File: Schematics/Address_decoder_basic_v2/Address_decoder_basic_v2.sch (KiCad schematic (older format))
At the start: 6 parts, among them J1 Address bus, J2 Clock, J3 ROM select, J4 RAM select, J5 VIA1 select, U1 74HC00

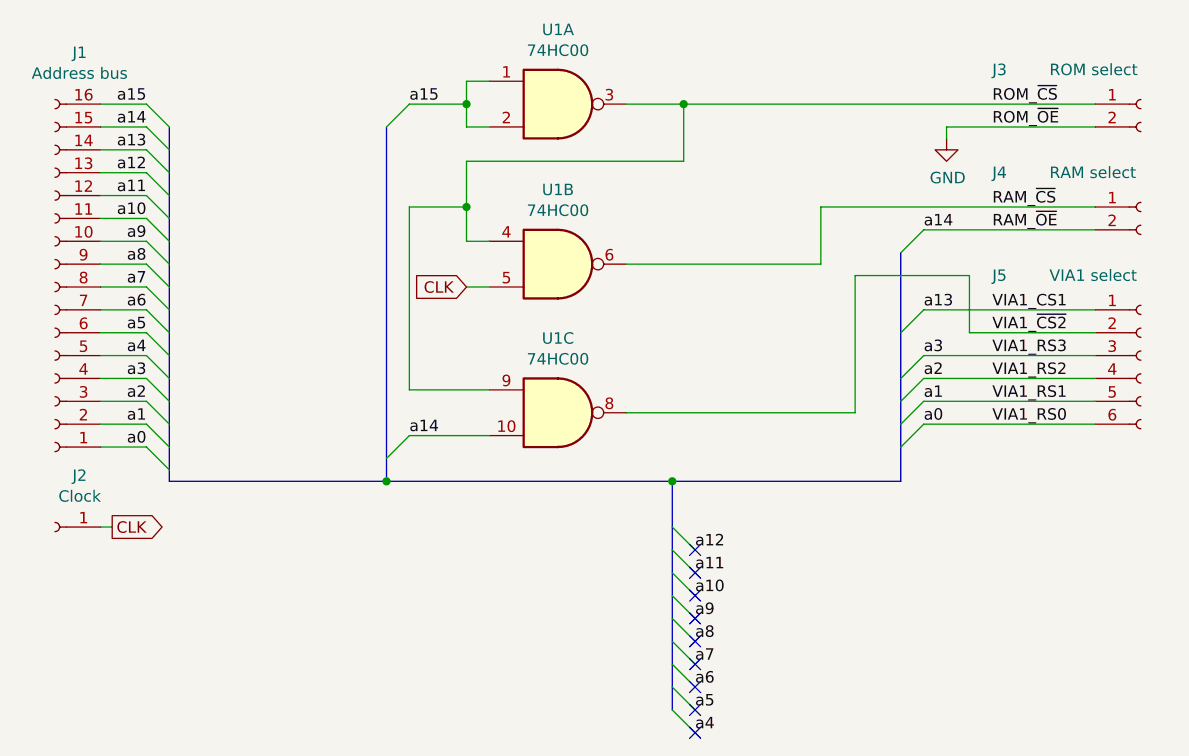
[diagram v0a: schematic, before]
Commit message: Updated v2 decoder schematic
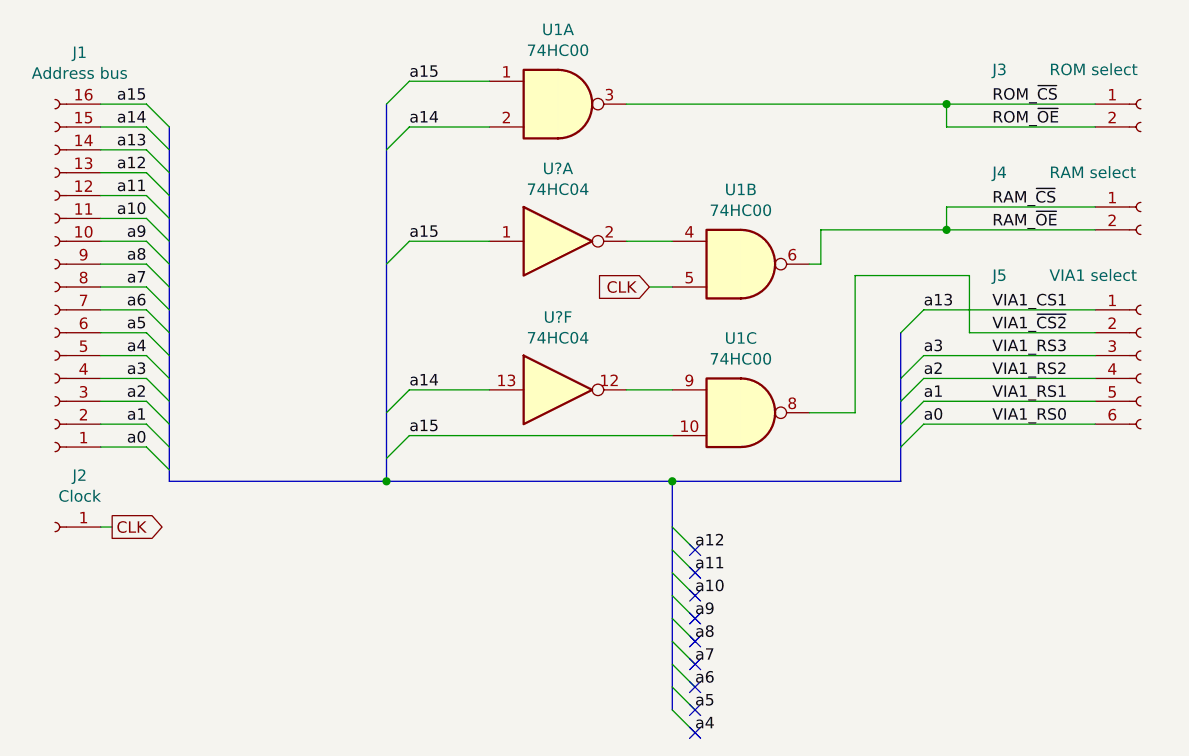
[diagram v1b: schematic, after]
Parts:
- added U? (x2): 74HC04, symbol 74xx:74HC04
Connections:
- net GND is gone; now on net ROM_~CS: J3.2 (Pin_2)
- net RAM_~CS: now also J4.2 (Pin_2)
- net ROM_~CS: no longer U1.4, U1.9
- net a15: now also U1.10, U?.1; no longer U1.2
- removed net RAM_~OE: J1.15 (Pin_15), J4.2 (Pin_2), U1.10
- new net: U1.4, U?.2
- new net: U1.9, U?.12
- new net a14: J1.15 (Pin_15), U1.2, U?.13
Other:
- moved on the sheet: U1B, U1C
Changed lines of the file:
@@
 Text Label 7400 4200 0    50   ~ 0
 VIA1_RS0
-Text Label 4850 2800 0    50   ~ 0
+Text Label 4850 3400 0    50   ~ 0
 a15
-Text Label 7100 3350 0    50   ~ 0
-a14
-$Comp
-L power:GND #PWR01
-U 1 1 5E0C3EF2
-P 7200 2950
-F 0 "#PWR01" H 7200 2700 50  0001 C CNN
-F 1 "GND" H 7205 2777 50  0000 C CNN
-F 2 "" H 7200 2950 50  0001 C CNN
-F 3 "" H 7200 2950 50  0001 C CNN
-	1    7200 2950
-	1    0    0    -1
-$EndComp
 Wire Wire Line
 	7200 2900 7850 2900
@@
 	1    0    0    -1
 $EndComp
-Wire Wire Line
-	5100 2800 5100 2900
-Wire Wire Line
-	5100 2900 5200 2900
-Wire Wire Line
-	5200 2700 5100 2700
-Wire Wire Line
-	5100 2700 5100 2800
-Connection ~ 5100 2800
-Wire Wire Line
-	7200 2900 7200 2950
-Entry Wire Line
-	4750 2900 4850 2800
+Entry Wire Line
+	4750 3500 4850 3400
 $Comp
 L 74xx:74HC00 U1
 U 2 1 5E0D5C1A
-P 5500 3500
-F 0 "U1" H 5500 3825 50  0000 C CNN
-F 1 "74HC00" H 5500 3734 50  0000 C CNN
-F 2 "" H 5500 3500 50  0001 C CNN
-F 3 "http://www.ti.com/lit/gpn/sn74hc00" H 5500 3500 50  0001 C CNN
-	2    5500 3500
+P 6300 3500
+F 0 "U1" H 6300 3825 50  0000 C CNN
+F 1 "74HC00" H 6300 3734 50  0000 C CNN
+F 2 "" H 6300 3500 50  0001 C CNN
+F 3 "http://www.ti.com/lit/gpn/sn74hc00" H 6300 3500 50  0001 C CNN
+	2    6300 3500
 	1    0    0    -1
 $EndComp
@@
 Wire Wire Line
 	7100 3900 7850 3900
-Wire Wire Line
-	5800 2800 6050 2800
-Wire Wire Line
-	6050 2800 6050 3050
-Wire Wire Line
-	6050 3050 5100 3050
-Wire Wire Line
-	5100 3050 5100 3250
-Wire Wire Line
-	5100 3400 5200 3400
-Connection ~ 6050 2800
-Wire Wire Line
-	6050 2800 7850 2800
-Text GLabel 5100 3600 0    50   Input ~ 0
+Text GLabel 5900 3600 0    50   Input ~ 0
 CLK
 Wire Wire Line
-	5100 3600 5200 3600
-Wire Wire Line
-	7100 3350 7850 3350
-Wire Wire Line
-	5800 3500 6650 3500
-Wire Wire Line
-	6650 3500 6650 3250
-Wire Wire Line
-	6650 3250 7850 3250
-Entry Wire Line
-	7000 3450 7100 3350
+	5900 3600 6000 3600
+Wire Wire Line
+	6600 3500 6650 3500
 Text Label 4850 4250 0    50   ~ 0
-a14
+a15
 $Comp
 L 74xx:74HC00 U1
 U 3 1 5E0E594E
-P 5500 4150
-F 0 "U1" H 5500 4475 50  0000 C CNN
-F 1 "74HC00" H 5500 4384 50  0000 C CNN
-F 2 "" H 5500 4150 50  0001 C CNN
-F 3 "http://www.ti.com/lit/gpn/sn74hc00" H 5500 4150 50  0001 C CNN
-	3    5500 4150
+P 6300 4150
+F 0 "U1" H 6300 4475 50  0000 C CNN
+F 1 "74HC00" H 6300 4384 50  0000 C CNN
+F 2 "" H 6300 4150 50  0001 C CNN
+F 3 "http://www.ti.com/lit/gpn/sn74hc00" H 6300 4150 50  0001 C CNN
+	3    6300 4150
 	1    0    0    -1
 $EndComp
@@
 	4750 4350 4850 4250
 Wire Wire Line
-	4850 4250 5200 4250
-Wire Wire Line
-	5200 4050 4850 4050
-Wire Wire Line
-	4850 4050 4850 3250
-Wire Wire Line
-	4850 3250 5100 3250
-Connection ~ 5100 3250
-Wire Wire Line
-	5100 3250 5100 3400
-Text Label 7100 3700 0    50   ~ 0
-a13
-Entry Wire Line
-	7000 3800 7100 3700
-Wire Wire Line
-	7100 3700 7850 3700
-Wire Wire Line
-	5800 4150 6800 4150
+	4850 4250 6000 4250
+Wire Wire Line
+	6000 4050 5800 4050
+Wire Wire Line
+	6600 4150 6800 4150
 Wire Bus Line
 	3800 4450 4750 4450
-Wire Wire Line
-	4850 2800 5100 2800
 Connection ~ 4750 4450
 Wire Bus Line
 	4750 4450 6000 4450
-Wire Wire Line
-	6800 4150 6800 3550
-Wire Wire Line
-	6800 3550 7300 3550
-Wire Wire Line
-	7300 3550 7300 3800
-Wire Wire Line
-	7300 3800 7850 3800
 Text Label 6100 4750 0    50   ~ 0
 a12
@@
 Wire Bus Line
 	6000 4450 7000 4450
-Wire Bus Line
-	4750 2900 4750 4450
-Wire Bus Line
-	7000 3450 7000 4450
+Wire Wire Line
+	7200 3250 7200 3350
+Wire Wire Line
+	7200 3250 7850 3250
+Wire Wire Line
+	7200 3350 7850 3350
+Wire Wire Line
+	7200 3350 6650 3350
+Wire Wire Line
+	6650 3350 6650 3500
+Connection ~ 7200 3350
+$Comp
+L 74xx:74HC04 U?
+U 1 1 5E0E0C1E
+P 5500 3400
+F 0 "U?" H 5500 3717 50  0000 C CNN
+F 1 "74HC04" H 5500 3626 50  0000 C CNN
+F 2 "" H 5500 3400 50  0001 C CNN
+F 3 "https://assets.nexperia.com/documents/data-sheet/74HC_HCT04.pdf" H 5500 3400 50  0001 C CNN
+	1    5500 3400
+	1    0    0    -1
+$EndComp
+Wire Wire Line
+	5800 2800 7200 2800
+Wire Wire Line
+	5800 3400 6000 3400
+Wire Wire Line
+	4850 3400 5200 3400
+Wire Wire Line
+	7200 2900 7200 2800
+Connection ~ 7200 2800
+Wire Wire Line
+	7200 2800 7850 2800
+Text Label 4850 2700 0    50   ~ 0
+a15
+Text Label 4850 2900 0    50   ~ 0
+a14
+Wire Wire Line
+	4850 2900 5200 2900
+Wire Wire Line
+	4850 2700 5200 2700
+Entry Wire Line
+	4750 2800 4850 2700
+Entry Wire Line
+	4750 3000 4850 2900
+$Comp
+L 74xx:74HC04 U?
+U 6 1 5E1086B3
+P 5500 4050
+F 0 "U?" H 5500 4367 50  0000 C CNN
+F 1 "74HC04" H 5500 4276 50  0000 C CNN
+F 2 "" H 5500 4050 50  0001 C CNN
+F 3 "https://assets.nexperia.com/documents/data-sheet/74HC_HCT04.pdf" H 5500 4050 50  0001 C CNN
+	6    5500 4050
+	1    0    0    -1
+$EndComp
+Text Label 4850 4050 0    50   ~ 0
+a14
+Entry Wire Line
+	4750 4150 4850 4050
+Wire Wire Line
+	4850 4050 5200 4050
+Wire Wire Line
+	6800 4150 6800 3550
+Wire Wire Line
+	7300 3800 7850 3800
+Wire Wire Line
+	6800 3550 7300 3550
+Wire Wire Line
+	7300 3550 7300 3800
+Entry Wire Line
+	7000 3800 7100 3700
+Text Label 7100 3700 0    50   ~ 0
+a13
 Wire Bus Line
 	6000 4450 6000 5450
 Wire Bus Line
+	7000 3800 7000 4450
+Wire Bus Line
+	4750 2800 4750 4450
+Wire Bus Line
 	3800 2900 3800 4450
+Wire Wire Line
+	7100 3700 7850 3700
 $EndSCHEMATC
